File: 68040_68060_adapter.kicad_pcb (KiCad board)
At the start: 2 copper layers, 59.1 x 95.6 mm, 33 parts, among them IC2 74F257, IC3 MC68060RCPGA_BIG, IC4 LMS1585-3.3, U4$1 4POL, U6$1 6POL

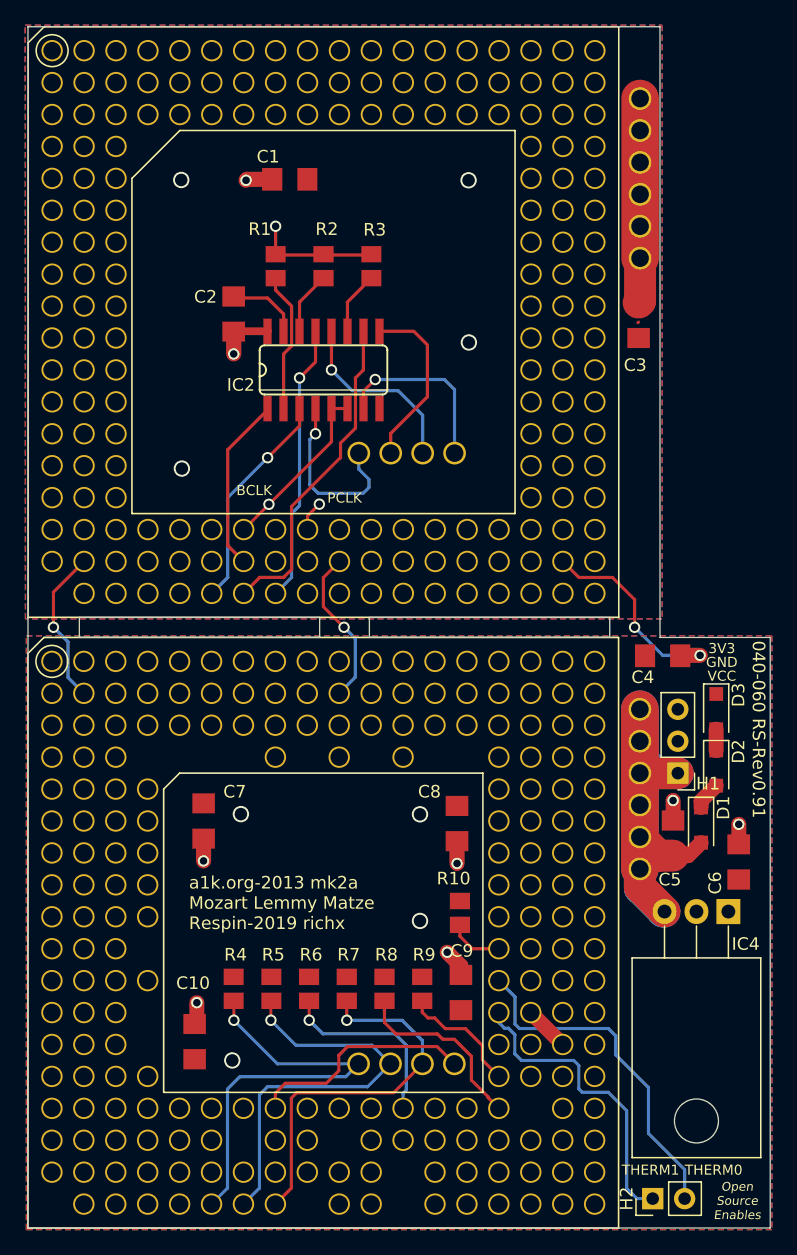
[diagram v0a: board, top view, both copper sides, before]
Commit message: Updated version 03-2021
- move inner connector in line with substrate
  and the pins of the socket. This allows to use sockets
  with 5 rows of pins without using a dremel
- move capacitors a bit more to the center to make space
  for 5 pin row sockets.
- use 0603 4.7k resistor networks instead of 0805 resistors
- move all three diodes in line for easier soldering
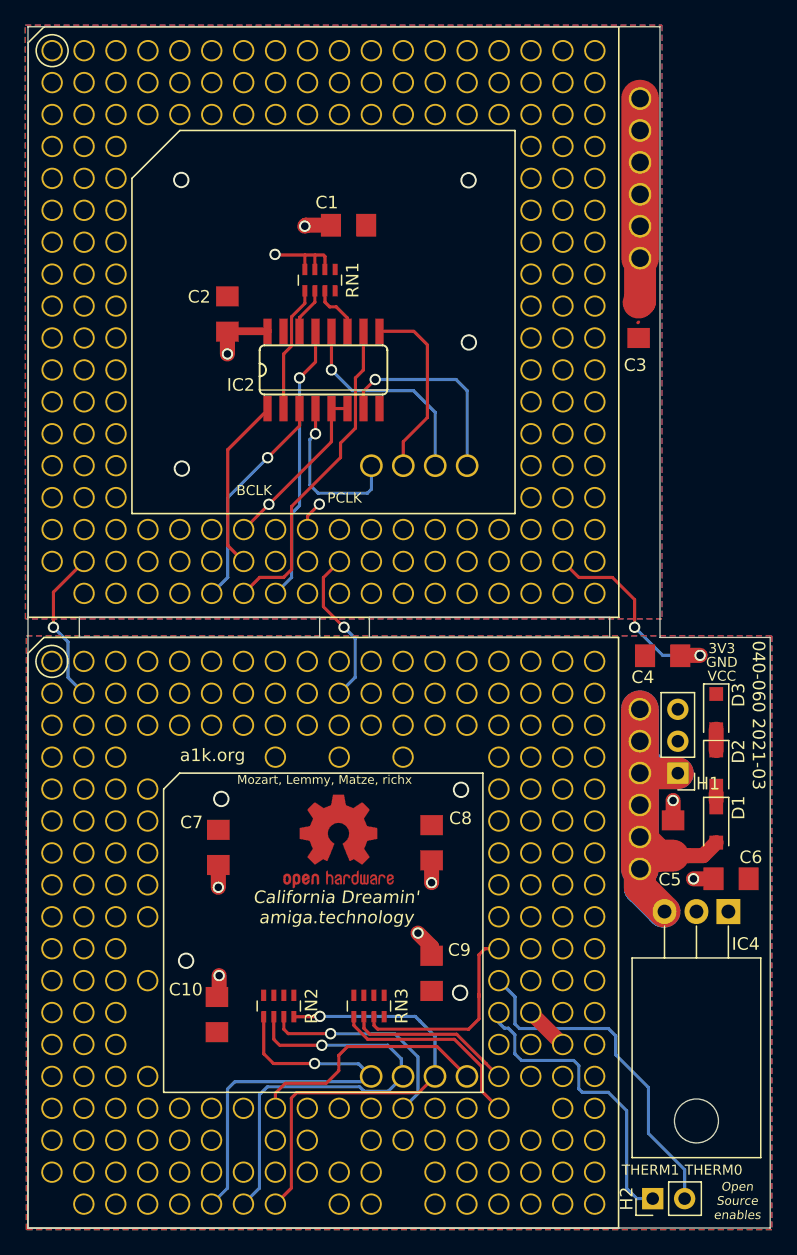
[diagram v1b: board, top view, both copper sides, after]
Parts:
- removed R1, R10, R2, R3, R4, R5, R6, R7, R8, R9: 4k7, Bot_68040_mk2a:M0805
- added REF**: OSHW-Logo2_9.8x8mm_Copper, KiCad/kicad-footprints/Symbol.pretty:OSHW-Logo2_9.8x8mm_Copper, F.Cu at (136.3, 108.4)
- added RN1: 4.7K, KiCad/kicad-footprints/Resistor_SMD.pretty:R_Array_Concave_4x0603, F.Cu at (134.9, 63.7)
- added RN2: 4.7k, KiCad/kicad-footprints/Resistor_SMD.pretty:R_Array_Concave_4x0603, F.Cu at (131.6, 121.5)
- added RN3: 4.7k, KiCad/kicad-footprints/Resistor_SMD.pretty:R_Array_Concave_4x0603, F.Cu at (138.8, 121.5)
- moved C1 5.93 mm to (137.2, 59.4)
- moved C10 2.79 mm to (126.7, 122.2)
- moved C9 2.78 mm to (143.8, 118.9)
- moved C8 2.54 mm to (143.8, 108.5)
- moved C7 2.41 mm to (126.8, 108.9)
- moved C6 1.47 mm to (167.6, 111.4), turned to 180 degrees
- moved D1 1.20 mm to (166.4, 107.1)
- moved C2 0.50 mm to (127.5, 66.4)
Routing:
- net CLA: track 4.41 -> 16.6 mm
- net IPL0: track 30.7 -> 36.4 mm
- net GND: track 62.5 -> 57.5 mm
- net SNOOP: track 10.3 -> 14.0 mm
- net 60_IPL0: track 14.9 -> 17.0 mm
- net 60_CLKEN: track 14.4 -> 16.4 mm
- net IPL1: track 33.2 -> 35.1 mm
- net TRA: track 15.2 -> 17.0 mm
- net ND1: track 2.22 -> 0.52 mm
- net VCC: track 32.9 -> 31.3 mm
- net CLKEN: track 18.3 -> 19.7 mm
- net VCC2: track 52.7 -> 53.9 mm
- net N$1: track 11.2 -> 10.1 mm
- net 60_IPL2: track 14.5 -> 13.4 mm
- net N$2: track 5.09 -> 4.27 mm
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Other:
- board text added: "040-060 2021-03"
- board text added: "California Dreamin' amiga.technology"
- board text added: "Mozart, Lemmy, Matze, richx"
- board text added: "Open Source enables"
- board text added: "a1k.org"
- board text removed: "040-060 RS-Rev0.91"
- board text removed: "Open Source Enables"
- board text removed: "a1k.org-2013 mk2a Mozart Lemmy Matze Respin-2019 richx"
